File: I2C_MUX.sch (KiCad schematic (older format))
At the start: 25 parts, among them U5 TCA9548ARGER

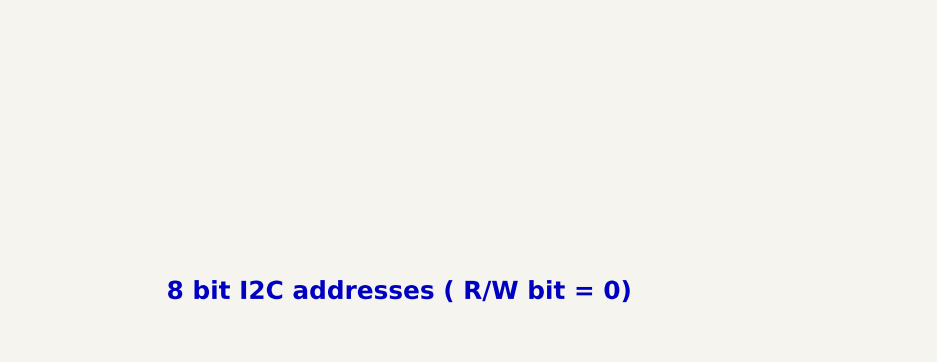
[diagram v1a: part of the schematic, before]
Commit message: SCH: Add 3rd INA219, remove +12VS power symbol
... also add some notes about current flow
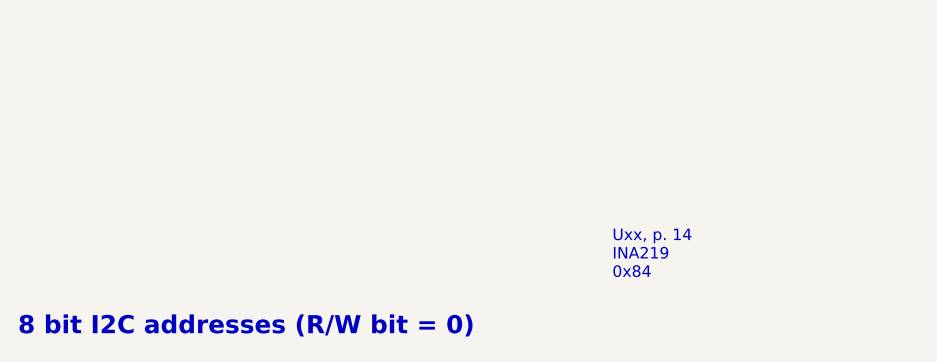
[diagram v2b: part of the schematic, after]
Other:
- note added: "8 bit I2C addresses (R/W bit = 0)"
- note added: "Uxx, p. 14\nINA219\n0x84"
- note removed: "8 bit I2C addresses ( R/W bit = 0)"
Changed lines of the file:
@@
 EndData
 $EndBitmap
-Text Notes 2600 7300 0    79   ~ 16
-8 bit I2C addresses ( R/W bit = 0)
+Text Notes 1950 7450 0    79   ~ 16
+8 bit I2C addresses (R/W bit = 0)
+Text Notes 4550 7200 0    50   ~ 0
+Uxx, p. 14\nINA219\n0x84
 $EndSCHEMATC

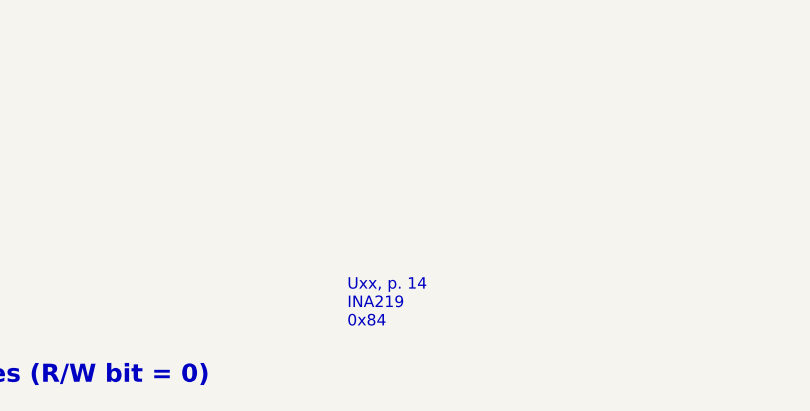
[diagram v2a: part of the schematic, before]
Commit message: SCH: PWR_FLAG cosmetics, update annotation
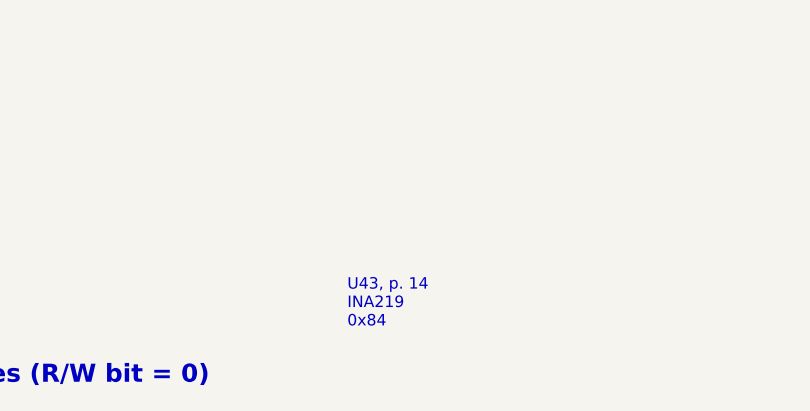
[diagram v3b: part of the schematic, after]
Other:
- note added: "U43, p. 14\nINA219\n0x84"
- note removed: "Uxx, p. 14\nINA219\n0x84"
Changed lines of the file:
@@
 8 bit I2C addresses (R/W bit = 0)
 Text Notes 4550 7200 0    50   ~ 0
-Uxx, p. 14\nINA219\n0x84
+U43, p. 14\nINA219\n0x84
 $EndSCHEMATC

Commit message: Convert all footprints to use Marble nickname
Includes both .sch and .lib files
Includes both bare footprint names and those with CERN-like nicknames
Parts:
- C40: footprint CAPC0603X33N -> Marble:CAPC0603X33N
- R274, R39, R40, R41, R42, R43, R44: footprint RESC1005X40N -> Marble:RESC1005X40N
- R45, R46, R47, R48, R49, R50, R51, R52, R53, R54, R55, R56, R57, R75, R83, R91: footprint Resistors SMD:RESC1005X40N -> Marble:RESC1005X40N
- U5: footprint ICs And Semiconductors SMD:QFN50P400X400X100-25N-S220 -> Marble:QFN50P400X400X100-25N-S220
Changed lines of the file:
@@
 F 0 "U5" H 5150 3978 50  0000 L CNN
 F 1 "TCA9548ARGER" H 5150 3887 50  0000 L CNN
-F 2 "ICs And Semiconductors SMD:QFN50P400X400X100-25N-S220" H 5150 1900 50  0001 C CNN
+F 2 "Marble:QFN50P400X400X100-25N-S220" H 5150 1900 50  0001 C CNN
 F 3 "http://www.ti.com/lit/ds/symlink/tca9548a.pdf" H 5200 3150 50  0001 C CNN
 F 4 "TCA9548ARGER" H 5150 2900 50  0001 C CNN "Manufacturer Part Number"
@@
 F 0 "R42" H 4950 3150 50  0000 C CNN
 F 1 "R0402_0R_JUMPER" H 4600 2990 60  0001 L CNN
-F 2 "RESC1005X40N" H 4600 2180 60  0001 L CNN
+F 2 "Marble:RESC1005X40N" H 4600 2180 60  0001 L CNN
 F 3 "\\\\cern.ch\\dfs\\Applications\\Altium\\Datasheets\\R0402_Phycomp_RC0402.pdf" H 4600 2810 60  0001 L CNN
 F 4 "0" H 4600 3150 50  0000 C CNN "~"
@@
 F 0 "R43" H 4950 3250 50  0000 C CNN
 F 1 "R0402_0R_JUMPER" H 4600 3090 60  0001 L CNN
-F 2 "RESC1005X40N" H 4600 2280 60  0001 L CNN
+F 2 "Marble:RESC1005X40N" H 4600 2280 60  0001 L CNN
 F 3 "\\\\cern.ch\\dfs\\Applications\\Altium\\Datasheets\\R0402_Phycomp_RC0402.pdf" H 4600 2910 60  0001 L CNN
 F 4 "0" H 4600 3250 50  0000 C CNN "~"
@@
 F 0 "R44" H 4950 3350 50  0000 C CNN
 F 1 "R0402_0R_JUMPER" H 4600 3190 60  0001 L CNN
-F 2 "RESC1005X40N" H 4600 2380 60  0001 L CNN
+F 2 "Marble:RESC1005X40N" H 4600 2380 60  0001 L CNN
 F 3 "\\\\cern.ch\\dfs\\Applications\\Altium\\Datasheets\\R0402_Phycomp_RC0402.pdf" H 4600 3010 60  0001 L CNN
 F 4 "0" H 4600 3350 50  0000 C CNN "~"
@@
 F 0 "R45" H 5900 2150 50  0000 C CNN
 F 1 "R0402_2K2_1%_0.0625W_100PPM" H 6000 1940 60  0001 L CNN
-F 2 "Resistors SMD:RESC1005X40N" H 6000 1130 60  0001 L CNN
+F 2 "Marble:RESC1005X40N" H 6000 1130 60  0001 L CNN
 F 3 "\\\\cern.ch\\dfs\\Applications\\Altium\\Datasheets\\R0402_Phycomp_RC0402.pdf" H 6000 1760 60  0001 L CNN
 F 4 "22k" H 6400 2150 50  0000 C CNN "~"
@@
 F 0 "R46" H 5900 2250 50  0000 C CNN
 F 1 "R0402_2K2_1%_0.0625W_100PPM" H 6000 2040 60  0001 L CNN
-F 2 "Resistors SMD:RESC1005X40N" H 6000 1230 60  0001 L CNN
+F 2 "Marble:RESC1005X40N" H 6000 1230 60  0001 L CNN
 F 3 "\\\\cern.ch\\dfs\\Applications\\Altium\\Datasheets\\R0402_Phycomp_RC0402.pdf" H 6000 1860 60  0001 L CNN
 F 4 "22k" H 6400 2250 50  0000 C CNN "~"
@@
 F 0 "R47" H 5900 2350 50  0000 C CNN
 F 1 "R0402_2K2_1%_0.0625W_100PPM" H 6000 2140 60  0001 L CNN
-F 2 "Resistors SMD:RESC1005X40N" H 6000 1330 60  0001 L CNN
+F 2 "Marble:RESC1005X40N" H 6000 1330 60  0001 L CNN
 F 3 "\\\\cern.ch\\dfs\\Applications\\Altium\\Datasheets\\R0402_Phycomp_RC0402.pdf" H 6000 1960 60  0001 L CNN
 F 4 "22k" H 6400 2350 50  0000 C CNN "~"
@@
 F 0 "R48" H 5900 2450 50  0000 C CNN
 F 1 "R0402_2K2_1%_0.0625W_100PPM" H 6000 2240 60  0001 L CNN
-F 2 "Resistors SMD:RESC1005X40N" H 6000 1430 60  0001 L CNN
+F 2 "Marble:RESC1005X40N" H 6000 1430 60  0001 L CNN
 F 3 "\\\\cern.ch\\dfs\\Applications\\Altium\\Datasheets\\R0402_Phycomp_RC0402.pdf" H 6000 2060 60  0001 L CNN
 F 4 "22k" H 6400 2450 50  0000 C CNN "~"
@@
 F 0 "R49" H 5900 2550 50  0000 C CNN
 F 1 "R0402_2K2_1%_0.0625W_100PPM" H 6000 2340 60  0001 L CNN
-F 2 "Resistors SMD:RESC1005X40N" H 6000 1530 60  0001 L CNN
+F 2 "Marble:RESC1005X40N" H 6000 1530 60  0001 L CNN
 F 3 "\\\\cern.ch\\dfs\\Applications\\Altium\\Datasheets\\R0402_Phycomp_RC0402.pdf" H 6000 2160 60  0001 L CNN
 F 4 "22k" H 6400 2550 50  0000 C CNN "~"
@@
 F 0 "R50" H 5900 2650 50  0000 C CNN
 F 1 "R0402_2K2_1%_0.0625W_100PPM" H 6000 2440 60  0001 L CNN
-F 2 "Resistors SMD:RESC1005X40N" H 6000 1630 60  0001 L CNN
+F 2 "Marble:RESC1005X40N" H 6000 1630 60  0001 L CNN
 F 3 "\\\\cern.ch\\dfs\\Applications\\Altium\\Datasheets\\R0402_Phycomp_RC0402.pdf" H 6000 2260 60  0001 L CNN
 F 4 "22k" H 6400 2650 50  0000 C CNN "~"
@@
 F 0 "R51" H 5900 2750 50  0000 C CNN
 F 1 "R0402_2K2_1%_0.0625W_100PPM" H 6000 2540 60  0001 L CNN
-F 2 "Resistors SMD:RESC1005X40N" H 6000 1730 60  0001 L CNN
+F 2 "Marble:RESC1005X40N" H 6000 1730 60  0001 L CNN
 F 3 "\\\\cern.ch\\dfs\\Applications\\Altium\\Datasheets\\R0402_Phycomp_RC0402.pdf" H 6000 2360 60  0001 L CNN
 F 4 "22k" H 6400 2750 50  0000 C CNN "~"
@@
 F 0 "R52" H 5900 2850 50  0000 C CNN
 F 1 "R0402_2K2_1%_0.0625W_100PPM" H 6000 2640 60  0001 L CNN
-F 2 "Resistors SMD:RESC1005X40N" H 6000 1830 60  0001 L CNN
+F 2 "Marble:RESC1005X40N" H 6000 1830 60  0001 L CNN
 F 3 "\\\\cern.ch\\dfs\\Applications\\Altium\\Datasheets\\R0402_Phycomp_RC0402.pdf" H 6000 2460 60  0001 L CNN
 F 4 "22k" H 6400 2850 50  0000 C CNN "~"
@@
 F 0 "R53" H 5900 2950 50  0000 C CNN
 F 1 "R0402_2K2_1%_0.0625W_100PPM" H 6000 2740 60  0001 L CNN
-F 2 "Resistors SMD:RESC1005X40N" H 6000 1930 60  0001 L CNN
+F 2 "Marble:RESC1005X40N" H 6000 1930 60  0001 L CNN
 F 3 "\\\\cern.ch\\dfs\\Applications\\Altium\\Datasheets\\R0402_Phycomp_RC0402.pdf" H 6000 2560 60  0001 L CNN
 F 4 "22k" H 6400 2950 50  0000 C CNN "~"
@@
 F 0 "R54" H 5900 3050 50  0000 C CNN
 F 1 "R0402_2K2_1%_0.0625W_100PPM" H 6000 2840 60  0001 L CNN
-F 2 "Resistors SMD:RESC1005X40N" H 6000 2030 60  0001 L CNN
+F 2 "Marble:RESC1005X40N" H 6000 2030 60  0001 L CNN
 F 3 "\\\\cern.ch\\dfs\\Applications\\Altium\\Datasheets\\R0402_Phycomp_RC0402.pdf" H 6000 2660 60  0001 L CNN
 F 4 "22k" H 6400 3050 50  0000 C CNN "~"
@@
 F 0 "R55" H 5900 3150 50  0000 C CNN
 F 1 "R0402_2K2_1%_0.0625W_100PPM" H 6000 2940 60  0001 L CNN
-F 2 "Resistors SMD:RESC1005X40N" H 6000 2130 60  0001 L CNN
+F 2 "Marble:RESC1005X40N" H 6000 2130 60  0001 L CNN
 F 3 "\\\\cern.ch\\dfs\\Applications\\Altium\\Datasheets\\R0402_Phycomp_RC0402.pdf" H 6000 2760 60  0001 L CNN
 F 4 "22k" H 6400 3150 50  0000 C CNN "~"
@@
 F 0 "R56" H 5900 3250 50  0000 C CNN
 F 1 "R0402_2K2_1%_0.0625W_100PPM" H 6000 3040 60  0001 L CNN
-F 2 "Resistors SMD:RESC1005X40N" H 6000 2230 60  0001 L CNN
+F 2 "Marble:RESC1005X40N" H 6000 2230 60  0001 L CNN
 F 3 "\\\\cern.ch\\dfs\\Applications\\Altium\\Datasheets\\R0402_Phycomp_RC0402.pdf" H 6000 2860 60  0001 L CNN
 F 4 "22k" H 6400 3250 50  0000 C CNN "~"
@@
 F 0 "R57" H 5900 3350 50  0000 C CNN
 F 1 "R0402_2K2_1%_0.0625W_100PPM" H 6000 3140 60  0001 L CNN
-F 2 "Resistors SMD:RESC1005X40N" H 6000 2330 60  0001 L CNN
+F 2 "Marble:RESC1005X40N" H 6000 2330 60  0001 L CNN
 F 3 "\\\\cern.ch\\dfs\\Applications\\Altium\\Datasheets\\R0402_Phycomp_RC0402.pdf" H 6000 2960 60  0001 L CNN
 F 4 "22k" H 6400 3350 50  0000 C CNN "~"
@@
 F 0 "R75" H 5900 3450 50  0000 C CNN
 F 1 "R0402_2K2_1%_0.0625W_100PPM" H 6000 3240 60  0001 L CNN
-F 2 "Resistors SMD:RESC1005X40N" H 6000 2430 60  0001 L CNN
+F 2 "Marble:RESC1005X40N" H 6000 2430 60  0001 L CNN
 F 3 "\\\\cern.ch\\dfs\\Applications\\Altium\\Datasheets\\R0402_Phycomp_RC0402.pdf" H 6000 3060 60  0001 L CNN
 F 4 "22k" H 6400 3450 50  0000 C CNN "~"
@@
 F 0 "R83" H 5900 3550 50  0000 C CNN
 F 1 "R0402_2K2_1%_0.0625W_100PPM" H 6000 3340 60  0001 L CNN
-F 2 "Resistors SMD:RESC1005X40N" H 6000 2530 60  0001 L CNN
+F 2 "Marble:RESC1005X40N" H 6000 2530 60  0001 L CNN
 F 3 "\\\\cern.ch\\dfs\\Applications\\Altium\\Datasheets\\R0402_Phycomp_RC0402.pdf" H 6000 3160 60  0001 L CNN
 F 4 "22k" H 6400 3550 50  0000 C CNN "~"
@@
 F 0 "R91" H 5900 3650 50  0000 C CNN
 F 1 "R0402_2K2_1%_0.0625W_100PPM" H 6000 3440 60  0001 L CNN
-F 2 "Resistors SMD:RESC1005X40N" H 6000 2630 60  0001 L CNN
+F 2 "Marble:RESC1005X40N" H 6000 2630 60  0001 L CNN
 F 3 "\\\\cern.ch\\dfs\\Applications\\Altium\\Datasheets\\R0402_Phycomp_RC0402.pdf" H 6000 3260 60  0001 L CNN
 F 4 "22k" H 6400 3650 50  0000 C CNN "~"
@@
 F 0 "R39" H 4150 1850 50  0000 L CNN
 F 1 "R0402_2K2_1%_0.0625W_100PPM" H 4050 1540 60  0001 L CNN
-F 2 "RESC1005X40N" H 4050 730 60  0001 L CNN
+F 2 "Marble:RESC1005X40N" H 4050 730 60  0001 L CNN
 F 3 "\\\\cern.ch\\dfs\\Applications\\Altium\\Datasheets\\R0402_Phycomp_RC0402.pdf" H 4050 1360 60  0001 L CNN
 F 4 "2k2" V 4350 1750 50  0000 L CNN "~"
@@
 F 0 "R40" H 4350 1850 50  0000 L CNN
 F 1 "R0402_2K2_1%_0.0625W_100PPM" H 4250 1540 60  0001 L CNN
-F 2 "RESC1005X40N" H 4250 730 60  0001 L CNN
+F 2 "Marble:RESC1005X40N" H 4250 730 60  0001 L CNN
 F 3 "\\\\cern.ch\\dfs\\Applications\\Altium\\Datasheets\\R0402_Phycomp_RC0402.pdf" H 4250 1360 60  0001 L CNN
 F 4 "2k2" V 4550 1750 50  0000 L CNN "~"
@@
 F 0 "R41" H 4550 1850 50  0000 L CNN
 F 1 "R0402_2K2_1%_0.0625W_100PPM" H 4450 1540 60  0001 L CNN
-F 2 "RESC1005X40N" H 4450 730 60  0001 L CNN
+F 2 "Marble:RESC1005X40N" H 4450 730 60  0001 L CNN
 F 3 "\\\\cern.ch\\dfs\\Applications\\Altium\\Datasheets\\R0402_Phycomp_RC0402.pdf" H 4450 1360 60  0001 L CNN
 F 4 "2k2" V 4750 1750 50  0000 L CNN "~"
@@
 F 0 "C40" V 4854 1910 50  0000 L CNN
 F 1 "CC0201_100NF_6.3V_10%_X5R" H 4750 1540 60  0001 L CNN
-F 2 "CAPC0603X33N" H 4750 730 60  0001 L CNN
+F 2 "Marble:CAPC0603X33N" H 4750 730 60  0001 L CNN
 F 3 "\\\\cern.ch\\dfs\\Applications\\Altium\\Datasheets\\CC0201_X5R_AVX.pdf" H 4750 1360 60  0001 L CNN
 F 4 "100nF" V 4945 1910 50  0000 L CNN "~"
@@
 F 0 "R274" H 4800 2750 50  0000 C CNN
 F 1 "R0402_0R_JUMPER" H 4650 2640 60  0001 L CNN
-F 2 "RESC1005X40N" H 4650 1830 60  0001 L CNN
+F 2 "Marble:RESC1005X40N" H 4650 1830 60  0001 L CNN
 F 3 "\\\\cern.ch\\dfs\\Applications\\Altium\\Datasheets\\R0402_Phycomp_RC0402.pdf" H 4650 2460 60  0001 L CNN
 F 4 "DNP" H 4800 2950 50  0000 C CNN "~"

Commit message: I2C pull-up resistors are truly 22k
Refresh from library to discard bogus 2K2 part number
R45 R46 R47 R48 R49 R50 R51 R52 R53 R54 R55 R56 R57 R75 R83 R91
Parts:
- R45, R46, R47, R48, R49, R50, R51, R52, R53, R54, R55, R56, R57, R75, R83, R91: value R0402_2K2_1%_0.0625W_100PPM -> R0402_22K_1%_0.0625W_100PPM; Comment =Value -> 22k; ComponentHeight ~~ -> (none); Database Table Name (none) -> Resistors SMD; Footprint Library (none) -> Resistors SMD; Library Name Resistors SMD -> Resistors.DbLib; PackageDescription ~~ -> (none); Sense Comment ~~ -> (none); Status Comment ~~ -> (none); Voltage ~~ -> (none)

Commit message: Get rid of most .DbLib suffixes in Library Name attributes
Enough that KiBoM no longer complains about them
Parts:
- R45, R46, R47, R48, R49, R50, R51, R52, R53, R54, R55, R56, R57, R75, R83, R91: Library Name Resistors.DbLib -> Resistors SMD

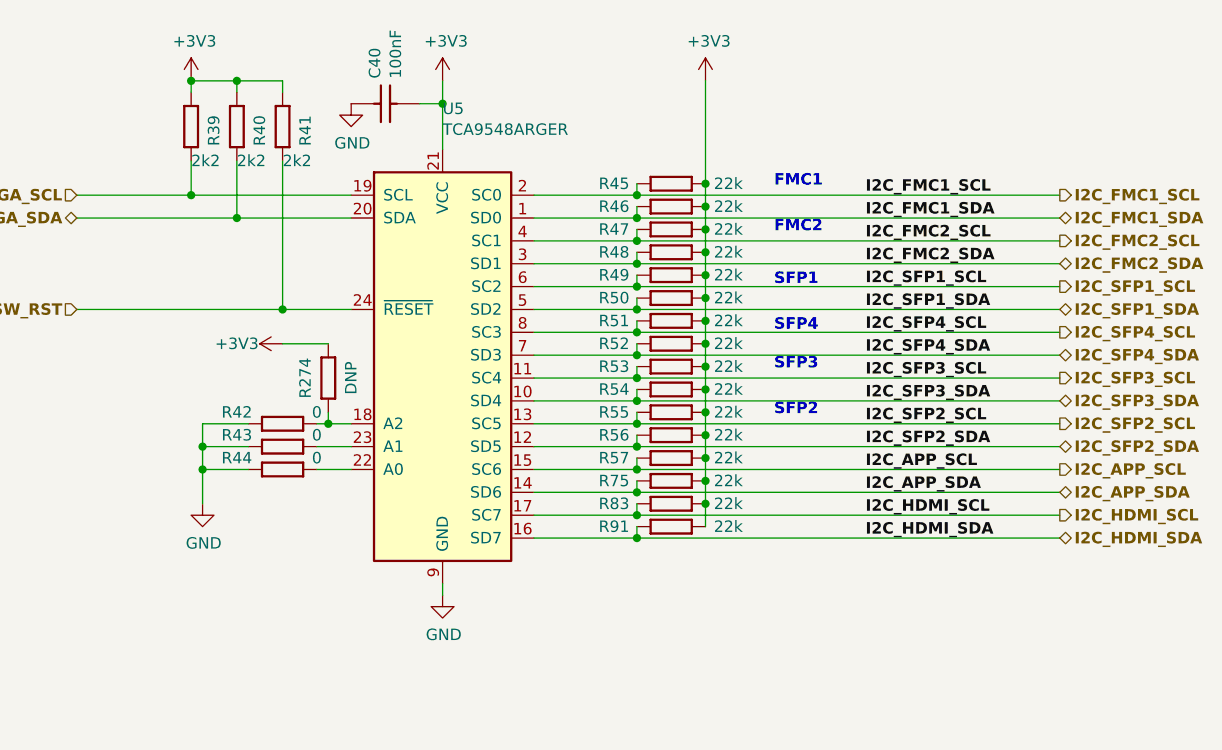
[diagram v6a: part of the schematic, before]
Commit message: replaced J14 connector, TCA9517 added, Exar chip hex files added
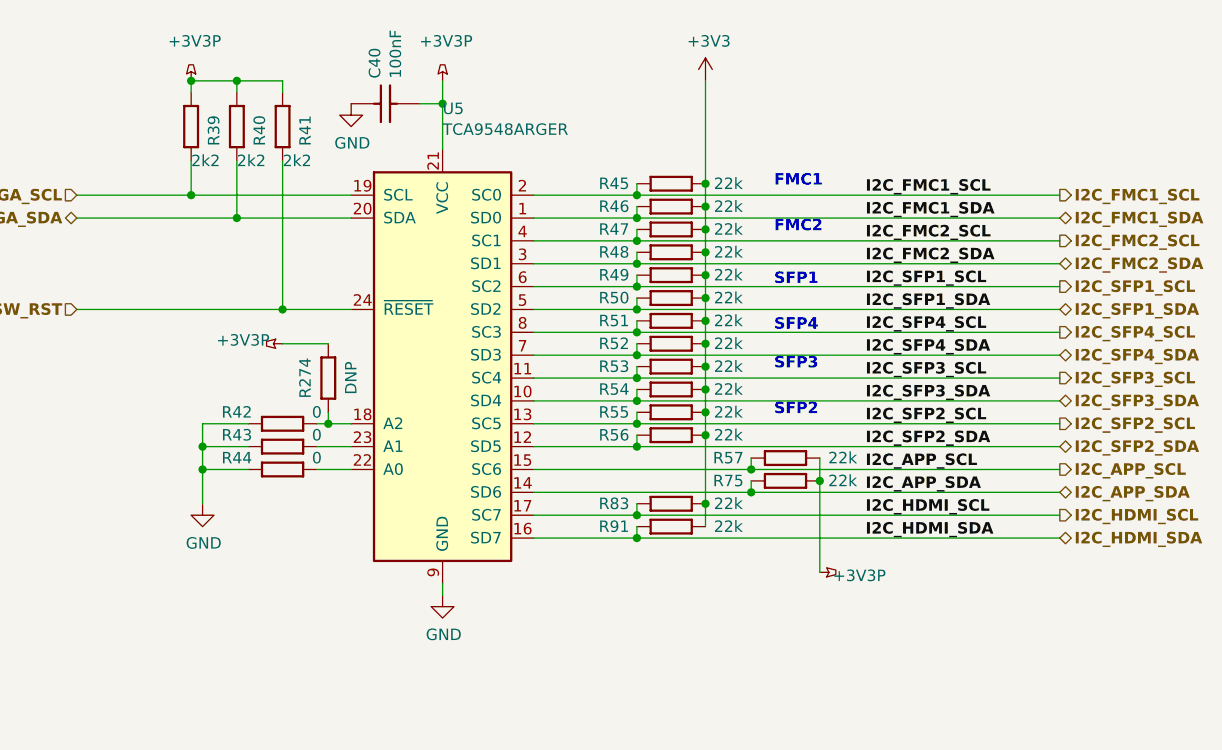
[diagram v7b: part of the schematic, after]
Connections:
- net +3V3: no longer C40.2, R274.1, R39.1, R40.1, R41.1, R57.2, R75.2, U5.21 (VCC)
- new net +3V3P: C40.2, R274.1, R39.1, R40.1, R41.1, R57.2, R75.2, U5.21 (VCC)
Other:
- moved on the sheet: R57, R75

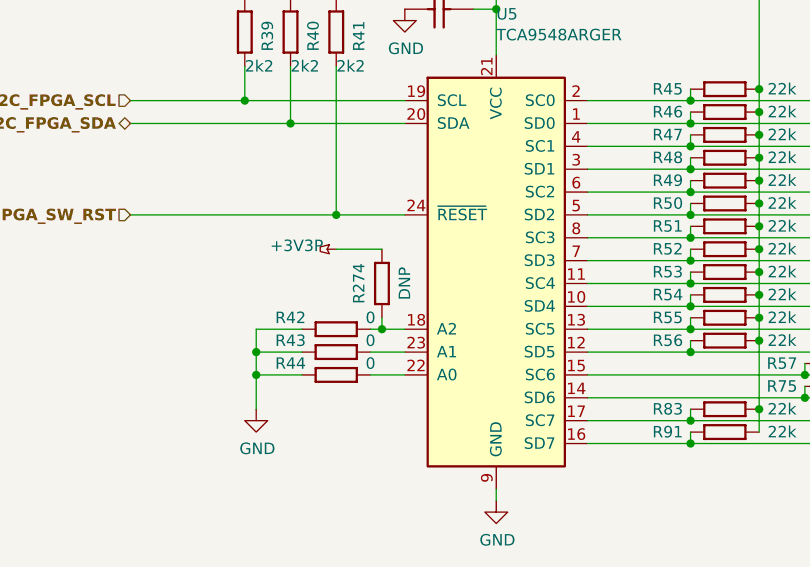
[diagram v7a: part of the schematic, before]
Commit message: Replace Val=DNP with actual value for 6 resistors
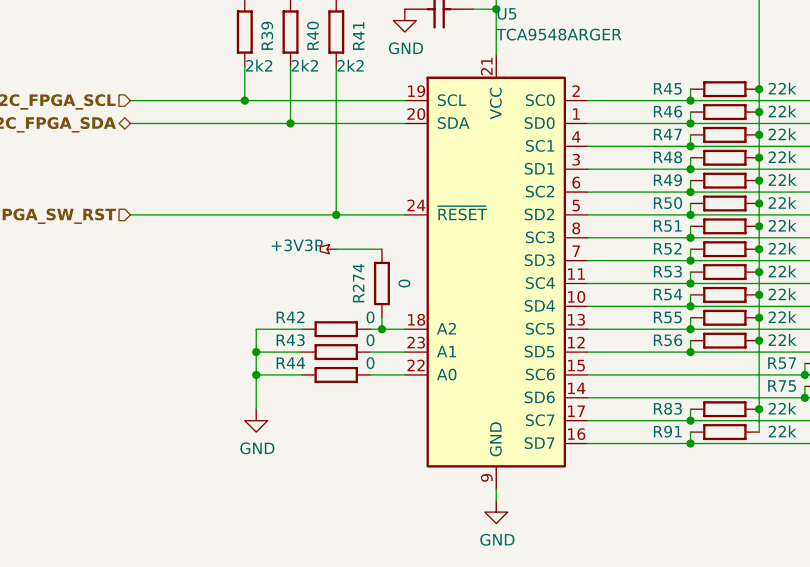
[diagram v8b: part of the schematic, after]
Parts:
- R274: ~ DNP -> (none)
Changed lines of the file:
@@
 F 2 "Marble:RESC1005X40N" H 4650 1830 60  0001 L CNN
 F 3 "\\\\cern.ch\\dfs\\Applications\\Altium\\Datasheets\\R0402_Phycomp_RC0402.pdf" H 4650 2460 60  0001 L CNN
-F 4 "DNP" H 4800 2950 50  0000 C CNN "~"
+F 4 "0" H 4800 2950 50  0000 C CNN "Val"
 F 5 "R0402_0R_JUMPER" H 4650 2370 60  0001 L CNN "Part Number"
 F 6 "Resistor" H 4650 2280 60  0001 L CNN "Library Ref"
